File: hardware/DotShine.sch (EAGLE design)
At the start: 56 parts, among them CN1 1X4-BIG, IC1 CAT24M010TS, IC3 SI1145, J3 USB-MICROB, U1 ATMEGA328P-MU-QFN32, U2 TMP102, U3 ATSHA204-TSU, X2 MC-RTC-RV-4162-C7-I2C, X3 S4B-ZR

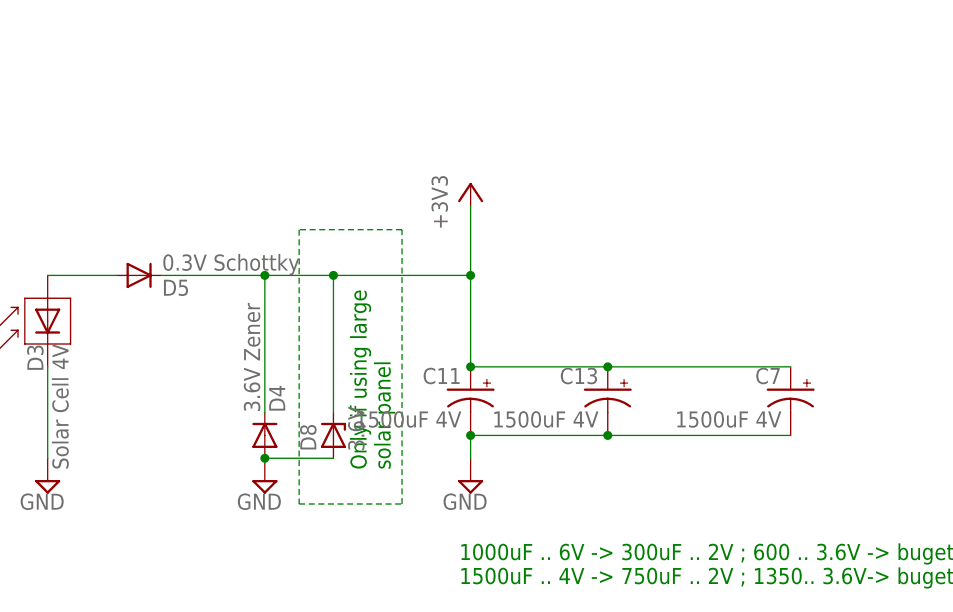
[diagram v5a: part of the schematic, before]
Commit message: Rem superfluous Zener for solar, out it to LDO
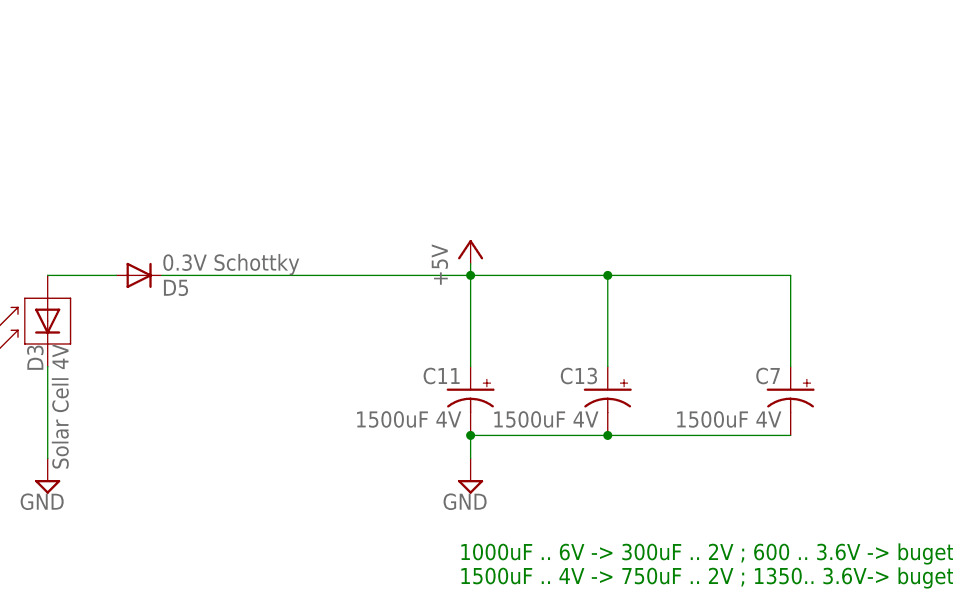
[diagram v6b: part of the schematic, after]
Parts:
- removed D4: 3.6V Zener, diode:DIODE-SOD523
- removed D8: 3.6V, diode:ZENER-DIODESOD80C
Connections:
- net +3V3: no longer C11.+, C13.+, C7.+, D4.C, D5.C, D8.C
- net +5V: now also C11.+, C13.+, C7.+, D5.C
- net GND: no longer D4.A, D8.A
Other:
- note removed: "Only if using large solar panel"
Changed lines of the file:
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@@
 <part name="U$3" library="pusbbutton_4x2_5" deviceset="PUSHBUTTON_4X2.5" device=""/>
 <part name="D3" library="SparkFun" deviceset="SOLAR-IXYS" device="-" value="Solar Cell 4V"/>
-<part name="D4" library="diode" deviceset="DIODE-" device="SOD523" value="3.6V Zener"/>
 <part name="SUPPLY33" library="supply2" deviceset="GND" device=""/>
 <part name="C11" library="adafruit" deviceset="CPOL-US" device="CT7343" value="1500uF 4V"/>
 <part name="SUPPLY35" library="supply2" deviceset="GND" device=""/>
 <part name="C13" library="adafruit" deviceset="CPOL-US" device="CT7343" value="1500uF 4V"/>
-<part name="SUPPLY34" library="supply2" deviceset="GND" device=""/>
 <part name="D5" library="diode" deviceset="DIODE-" device="SOD523" value="0.3V Schottky"/>
 <part name="IC3" library="silabs" deviceset="SI114*" device="" technology="5"/>
@@
 <part name="TP1" library="SparkFun" deviceset="TEST-POINT" device="3"/>
 <part name="C7" library="adafruit" deviceset="CPOL-US" device="CT7343" value="1500uF 4V"/>
-<part name="+3V3" library="supply1" deviceset="+3V3" device=""/>
 <part name="D6" library="diode" deviceset="DIODE-" device="SOD523" value="0.3V Schottky"/>
 <part name="J1" library="solderjumper" deviceset="SOLDERJUMPER.2" device=".MED"/>
-<part name="D8" library="diode" deviceset="ZENER-DIODE" device="SOD80C" value="3.6V"/>
 <part name="P+1" library="supply1" deviceset="+5V" device=""/>
+<part name="P+5" library="supply1" deviceset="+5V" device=""/>
 </parts>
 <sheets>
@@
 <text x="30.48" y="-243.84" size="1.778" layer="91">1000uF .. 6V -&gt; 300uF .. 2V ; 600 .. 3.6V -&gt; buget: 600-300 = 300uF
 1500uF .. 4V -&gt; 750uF .. 2V ; 1350.. 3.6V-&gt; buget: 1350-750 = 600uF</text>
-<text x="22.86" y="-231.14" size="1.778" layer="91" rot="R90">Only if using large
-solar panel</text>
 </plain>
 <instances>
@@
 <instance part="U$3" gate="G$1" x="57.15" y="-5.08" rot="R90"/>
 <instance part="D3" gate="G$1" x="-15.24" y="-214.63" rot="MR270"/>
-<instance part="D4" gate="G$1" x="8.89" y="-227.33" rot="MR90"/>
 <instance part="SUPPLY33" gate="GND" x="-15.24" y="-232.41" rot="MR0"/>
 <instance part="C11" gate="G$1" x="31.75" y="-222.25" rot="MR0"/>
 <instance part="SUPPLY35" gate="GND" x="31.75" y="-232.41" rot="MR0"/>
 <instance part="C13" gate="G$1" x="46.99" y="-222.25" rot="MR0"/>
-<instance part="SUPPLY34" gate="GND" x="8.89" y="-232.41" rot="MR0"/>
 <instance part="D5" gate="G$1" x="-5.08" y="-209.55" rot="MR180"/>
 <instance part="IC3" gate="G$1" x="180.34" y="-215.9"/>
@@
 <instance part="TP1" gate="G$1" x="-50.8" y="68.58" rot="R180"/>
 <instance part="C7" gate="G$1" x="67.31" y="-222.25" rot="MR0"/>
-<instance part="+3V3" gate="G$1" x="31.75" y="-199.39"/>
 <instance part="D6" gate="G$1" x="165.1" y="-35.56" rot="MR180"/>
 <instance part="J1" gate="G$1" x="165.1" y="-30.48"/>
-<instance part="D8" gate="G$1" x="16.51" y="-227.33" rot="R90"/>
 <instance part="P+1" gate="1" x="114.3" y="142.24" rot="R90"/>
+<instance part="P+5" gate="1" x="31.75" y="-205.74"/>
 </instances>
 <busses>
@@
 <wire x1="67.31" y1="-227.33" x2="46.99" y2="-227.33" width="0.1524" layer="91"/>
 <junction x="46.99" y="-227.33"/>
-</segment>
-<segment>
-<pinref part="D4" gate="G$1" pin="A"/>
-<pinref part="SUPPLY34" gate="GND" pin="GND"/>
-<wire x1="16.51" y1="-229.87" x2="8.89" y2="-229.87" width="0.1524" layer="91"/>
-<junction x="8.89" y="-229.87"/>
-<pinref part="D8" gate="G$1" pin="A"/>
 </segment>
 <segment>
@@
 </segment>
 <segment>
-<pinref part="C13" gate="G$1" pin="+"/>
-<pinref part="C11" gate="G$1" pin="+"/>
-<wire x1="46.99" y1="-219.71" x2="31.75" y2="-219.71" width="0.1524" layer="91"/>
-<junction x="31.75" y="-219.71"/>
-<wire x1="31.75" y1="-209.55" x2="31.75" y2="-219.71" width="0.1524" layer="91"/>
-<pinref part="D5" gate="G$1" pin="C"/>
-<wire x1="-2.54" y1="-209.55" x2="8.89" y2="-209.55" width="0.1524" layer="91"/>
-<pinref part="D4" gate="G$1" pin="C"/>
-<wire x1="8.89" y1="-209.55" x2="16.51" y2="-209.55" width="0.1524" layer="91"/>
-<wire x1="16.51" y1="-209.55" x2="31.75" y2="-209.55" width="0.1524" layer="91"/>
-<wire x1="8.89" y1="-224.79" x2="8.89" y2="-209.55" width="0.1524" layer="91"/>
-<junction x="8.89" y="-209.55"/>
-<pinref part="C7" gate="G$1" pin="+"/>
-<wire x1="67.31" y1="-219.71" x2="46.99" y2="-219.71" width="0.1524" layer="91"/>
-<junction x="46.99" y="-219.71"/>
-<pinref part="+3V3" gate="G$1" pin="+3V3"/>
-<wire x1="31.75" y1="-201.93" x2="31.75" y2="-209.55" width="0.1524" layer="91"/>
-<junction x="31.75" y="-209.55"/>
-<pinref part="D8" gate="G$1" pin="C"/>
-<wire x1="16.51" y1="-224.79" x2="16.51" y2="-209.55" width="0.1524" layer="91"/>
-<junction x="16.51" y="-209.55"/>
-</segment>
-<segment>
 <pinref part="J1" gate="G$1" pin="2"/>
 <pinref part="D6" gate="G$1" pin="C"/>
@@
 <pinref part="LED2" gate="G$1" pin="A"/>
 <wire x1="127" y1="142.24" x2="116.84" y2="142.24" width="0.1524" layer="91"/>
+</segment>
+<segment>
+<pinref part="D5" gate="G$1" pin="C"/>
+<pinref part="P+5" gate="1" pin="+5V"/>
+<wire x1="-2.54" y1="-209.55" x2="31.75" y2="-209.55" width="0.1524" layer="91"/>
+<wire x1="31.75" y1="-209.55" x2="31.75" y2="-208.28" width="0.1524" layer="91"/>
+<pinref part="C11" gate="G$1" pin="+"/>
+<wire x1="31.75" y1="-209.55" x2="31.75" y2="-219.71" width="0.1524" layer="91"/>
+<junction x="31.75" y="-209.55"/>
+<pinref part="C13" gate="G$1" pin="+"/>
+<wire x1="46.99" y1="-219.71" x2="46.99" y2="-209.55" width="0.1524" layer="91"/>
+<wire x1="46.99" y1="-209.55" x2="31.75" y2="-209.55" width="0.1524" layer="91"/>
+<pinref part="C7" gate="G$1" pin="+"/>
+<wire x1="67.31" y1="-219.71" x2="67.31" y2="-209.55" width="0.1524" layer="91"/>
+<wire x1="67.31" y1="-209.55" x2="46.99" y2="-209.55" width="0.1524" layer="91"/>
+<junction x="46.99" y="-209.55"/>
 </segment>
 </net>
@@
 </segment>
 </net>
-<net name="N$33" class="0">
-<segment>
-<wire x1="12.7" y1="-204.47" x2="12.7" y2="-234.95" width="0.1524" layer="91" style="shortdash"/>
-<wire x1="12.7" y1="-234.95" x2="24.13" y2="-234.95" width="0.1524" layer="91" style="shortdash"/>
-<wire x1="24.13" y1="-234.95" x2="24.13" y2="-204.47" width="0.1524" layer="91" style="shortdash"/>
-<wire x1="24.13" y1="-204.47" x2="12.7" y2="-204.47" width="0.1524" layer="91" style="shortdash"/>
-</segment>
-</net>

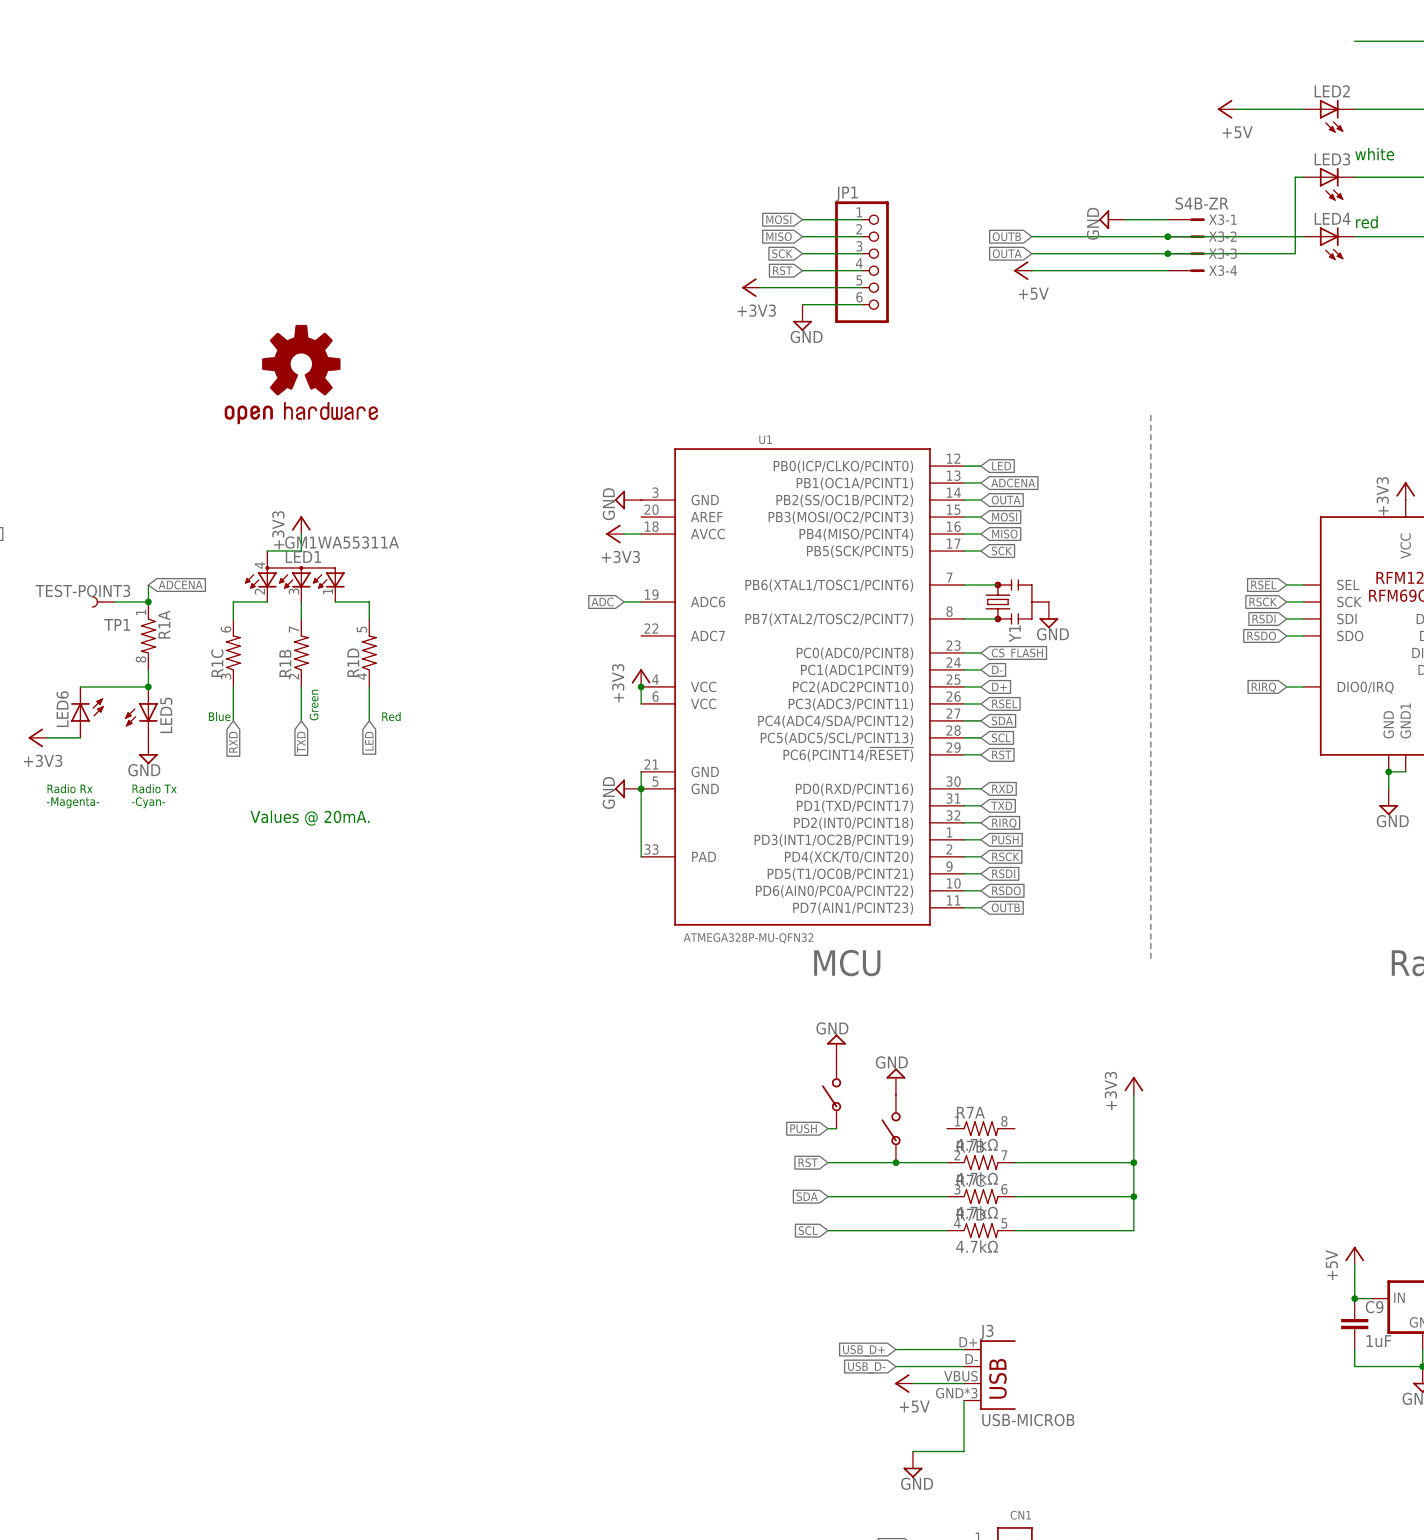
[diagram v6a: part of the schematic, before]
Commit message: Separate USB Led from solar
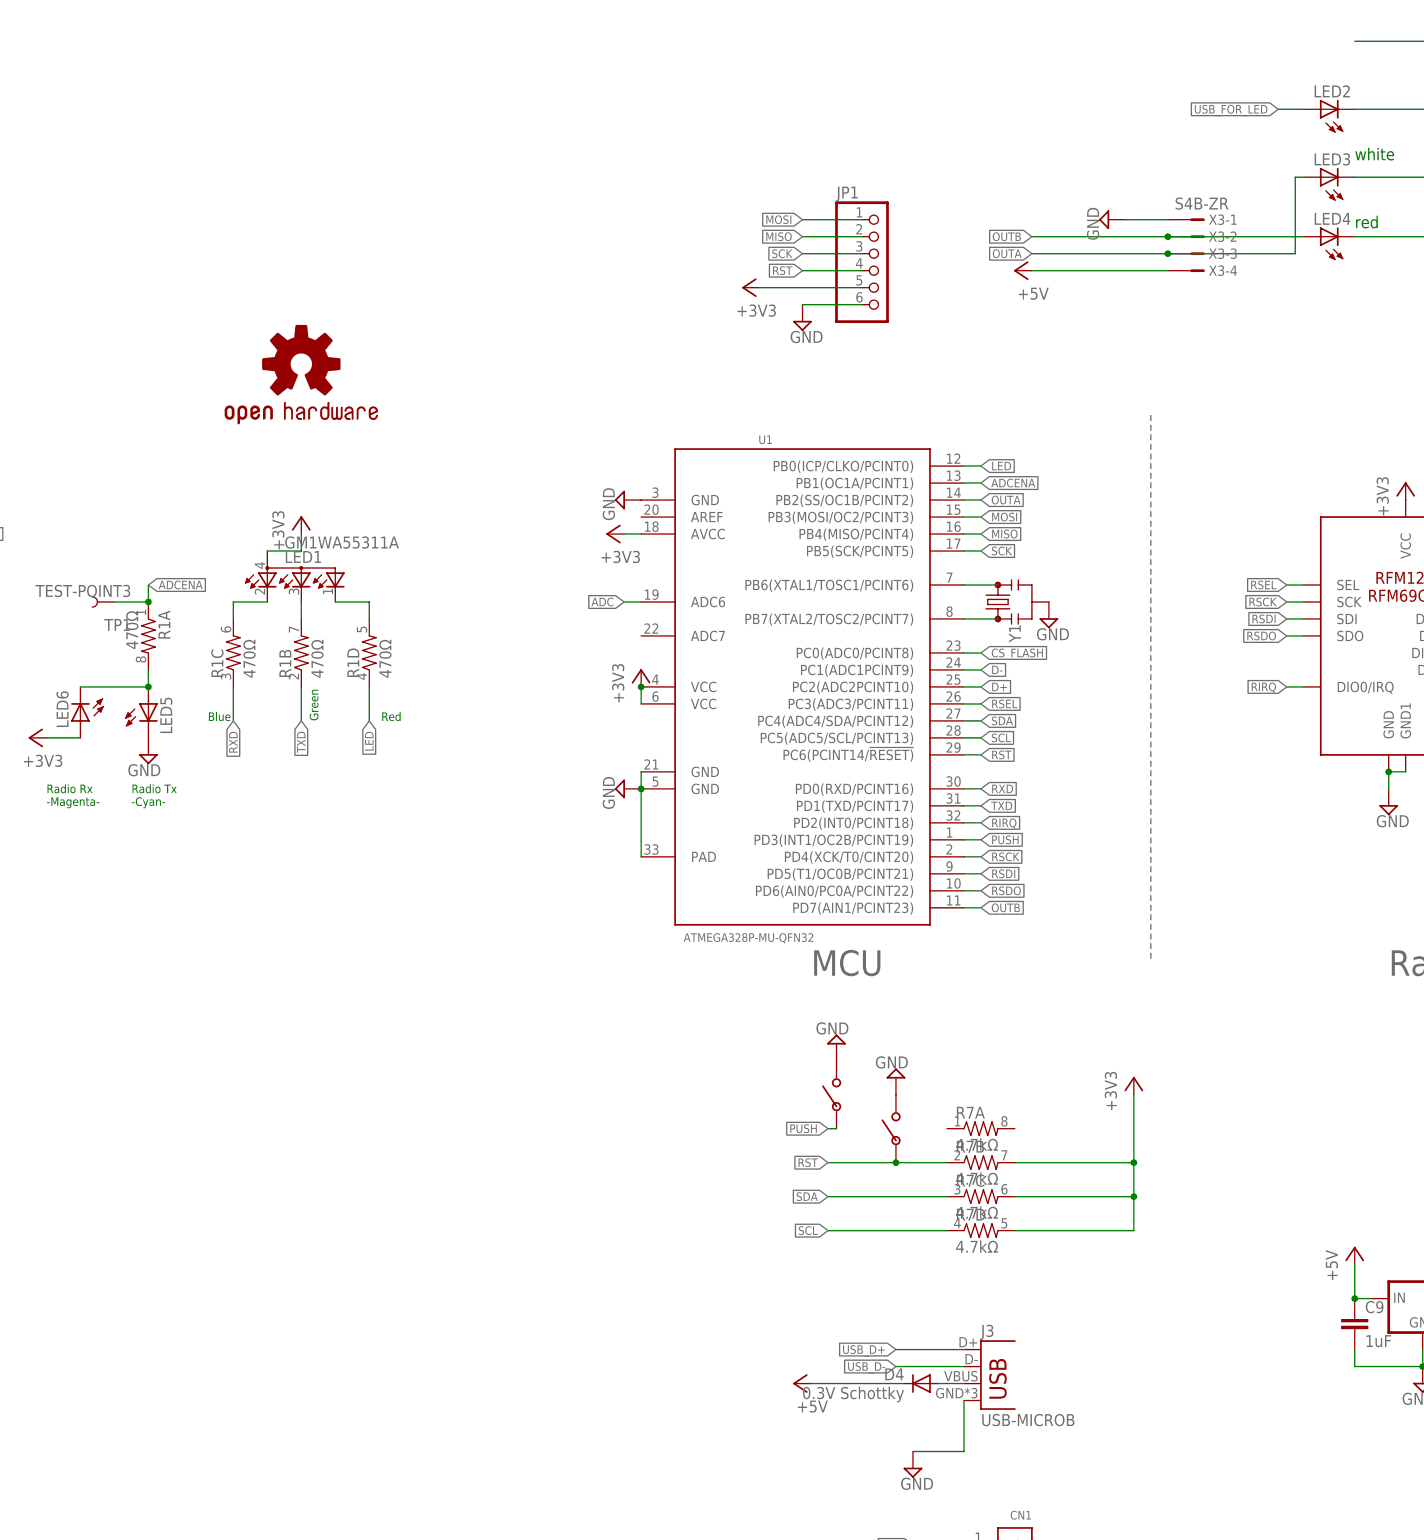
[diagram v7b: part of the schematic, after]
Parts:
- added D4: 0.3V Schottky, diode:DIODE-SOD523
- R1: value (none) -> 470Ω
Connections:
- new net USB_FOR_LED: D4.A, J3.VBUS, LED2.A
- net +5V: now also D4.C; no longer J3.VBUS, LED2.A
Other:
- note removed: "Values @ 20mA."
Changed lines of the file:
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@@
 <part name="P+4" library="supply1" deviceset="+5V" device=""/>
 <part name="C1" library="rcl" deviceset="C-EU" device="C0603" value="1uF"/>
-<part name="R1" library="SparkFun" deviceset="RESISTOR-ARRAY" device="0603-ARV"/>
+<part name="R1" library="SparkFun" deviceset="RESISTOR-ARRAY" device="0603-ARV" value="470Ω"/>
 <part name="U2" library="SparkFun" deviceset="TMP102" device=""/>
 <part name="SUPPLY15" library="supply2" deviceset="GND" device=""/>
@@
 <part name="D6" library="diode" deviceset="DIODE-" device="SOD523" value="0.3V Schottky"/>
 <part name="J1" library="solderjumper" deviceset="SOLDERJUMPER.2" device=".MED"/>
-<part name="P+1" library="supply1" deviceset="+5V" device=""/>
 <part name="P+5" library="supply1" deviceset="+5V" device=""/>
+<part name="D4" library="diode" deviceset="DIODE-" device="SOD523" value="0.3V Schottky"/>
 </parts>
 <sheets>
@@
 <text x="53.34" y="12.7" size="3.81" layer="95">MCU</text>
 <text x="139.7" y="12.7" size="3.81" layer="95">Radio</text>
-<text x="-30.48" y="35.56" size="1.778" layer="91">Values @ 20mA.</text>
 <text x="-36.83" y="50.8" size="1.27" layer="91">Blue</text>
 <text x="-20.32" y="50.8" size="1.27" layer="91" rot="R90">Green</text>
@@
 <instance part="SUPPLY9" gate="GND" x="160.02" y="123.19" rot="R90"/>
 <instance part="LED4" gate="G$1" x="129.54" y="123.19" rot="R90"/>
-<instance part="P+3" gate="1" x="66.04" y="-48.26" rot="R90"/>
+<instance part="P+3" gate="1" x="50.8" y="-48.26" rot="R90"/>
 <instance part="SUPPLY10" gate="GND" x="68.58" y="-60.96"/>
 <instance part="J3" gate="G$1" x="78.74" y="-50.8"/>
@@
 <instance part="D6" gate="G$1" x="165.1" y="-35.56" rot="MR180"/>
 <instance part="J1" gate="G$1" x="165.1" y="-30.48"/>
-<instance part="P+1" gate="1" x="114.3" y="142.24" rot="R90"/>
 <instance part="P+5" gate="1" x="31.75" y="-205.74"/>
+<instance part="D4" gate="G$1" x="69.85" y="-48.26" rot="MR0"/>
 </instances>
 <busses>
@@
 </segment>
 <segment>
-<wire x1="76.2" y1="-48.26" x2="68.58" y2="-48.26" width="0.1524" layer="91"/>
-<pinref part="P+3" gate="1" pin="+5V"/>
-<pinref part="J3" gate="G$1" pin="VBUS"/>
-</segment>
-<segment>
 <pinref part="P+4" gate="1" pin="+5V"/>
 <wire x1="134.62" y1="-30.48" x2="134.62" y2="-35.56" width="0.1524" layer="91"/>
@@
 <pinref part="C9" gate="G$1" pin="1"/>
 <junction x="134.62" y="-35.56"/>
-</segment>
-<segment>
-<pinref part="P+1" gate="1" pin="+5V"/>
-<pinref part="LED2" gate="G$1" pin="A"/>
-<wire x1="127" y1="142.24" x2="116.84" y2="142.24" width="0.1524" layer="91"/>
 </segment>
 <segment>
@@
 <junction x="46.99" y="-209.55"/>
 </segment>
+<segment>
+<pinref part="D4" gate="G$1" pin="C"/>
+<pinref part="P+3" gate="1" pin="+5V"/>
+<wire x1="67.31" y1="-48.26" x2="53.34" y2="-48.26" width="0.1524" layer="91"/>
+</segment>
 </net>
 <net name="N$7" class="0">
@@
 </segment>
 </net>
+<net name="USB_FOR_LED" class="0">
+<segment>
+<pinref part="J3" gate="G$1" pin="VBUS"/>
+<pinref part="D4" gate="G$1" pin="A"/>
+<wire x1="76.2" y1="-48.26" x2="72.39" y2="-48.26" width="0.1524" layer="91"/>
+</segment>
+<segment>
+<pinref part="LED2" gate="G$1" pin="A"/>
+<wire x1="127" y1="142.24" x2="123.19" y2="142.24" width="0.1524" layer="91"/>
+<label x="123.19" y="142.24" size="1.27" layer="95" rot="R180" xref="yes"/>
+</segment>
+</net>
